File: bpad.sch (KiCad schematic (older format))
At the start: 49 parts, among them J1 USB_B_Mini, SW1 Num, SW10 *, SW11 9, SW12 6, SW13 3, SW14 Del, SW15 -, SW16 +, SW17 Ent, SW2 7, SW3 4, SW4 1, SW5 0, SW6 /, SW7 8, SW8 5, SW9 2, U1 ATmega32U4-AU, Y1 16MHz

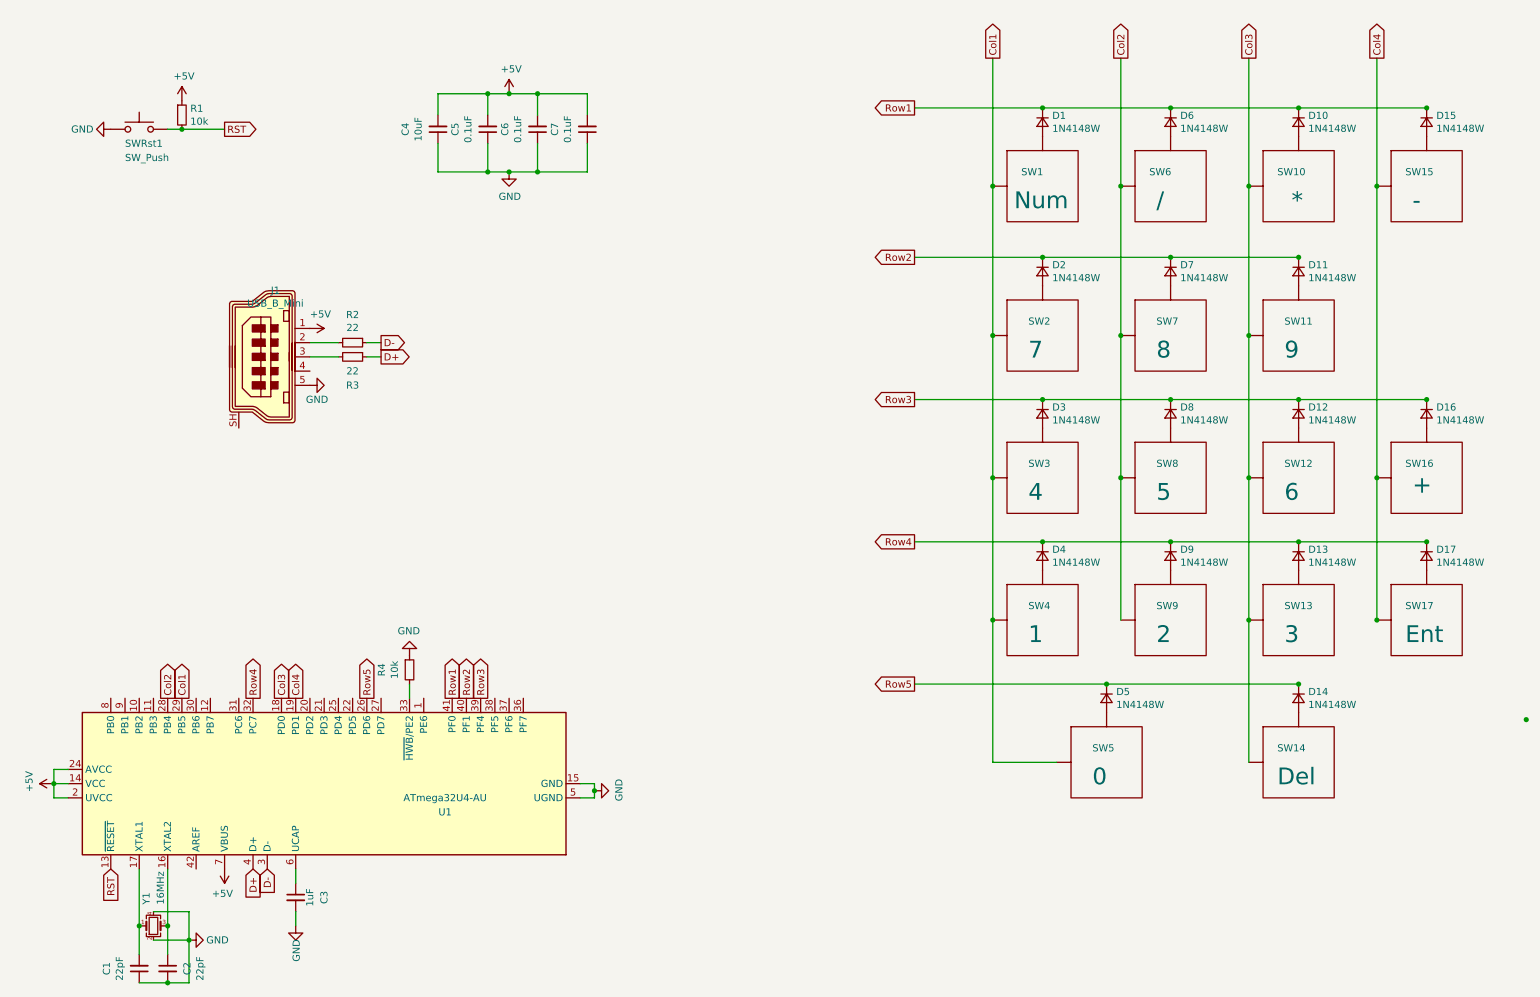
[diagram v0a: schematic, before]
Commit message: started again on the layout
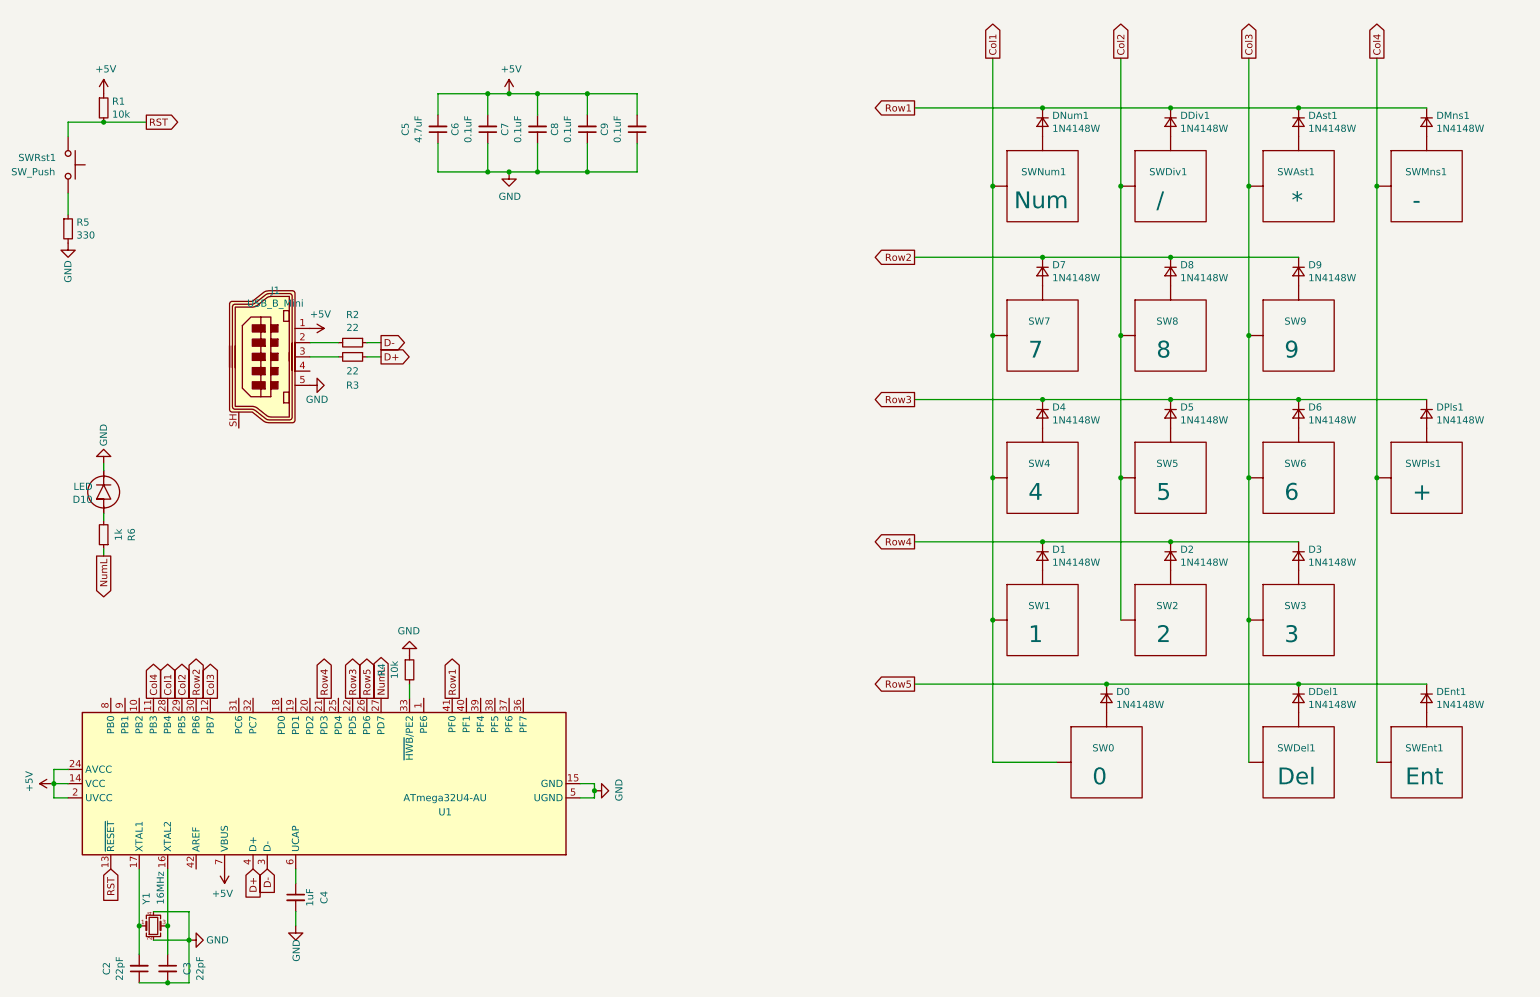
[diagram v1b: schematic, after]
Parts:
- added C9: 0.1uF, Capacitor_SMD:C_0603_1608Metric_Pad1.05x0.95mm_HandSolder, symbol Device:C_Small
- added D10: LED, AcheronComponents:LED_THT_2.54mm, symbol Acheron:LED
- added R5: 330, Resistor_SMD:R_0603_1608Metric_Pad1.05x0.95mm_HandSolder, symbol Device:R_Small
- added R6: 1k, Resistor_SMD:R_0603_1608Metric_Pad1.05x0.95mm_HandSolder, symbol Device:R_Small
- C5: renamed from C4; value 10uF -> 4.7uF
- renumbered C1 to C2, C2 to C3, C3 to C4, C5 to C6, C6 to C7, C7 to C8, D5 to D0, D4 to D1, D9 to D2, D13 to D3, D3 to D4, D8 to D5, D12 to D6, D2 to D7, D7 to D8, D11 to D9, D10 to DAst1, D14 to DDel1, D6 to DDiv1, D17 to DEnt1, D15 to DMns1, D1 to DNum1, D16 to DPls1, SW5 to SW0, SW4 to SW1, SW9 to SW2, SW13 to SW3, SW3 to SW4, SW8 to SW5, SW12 to SW6, SW2 to SW7, SW7 to SW8, SW11 to SW9, SW10 to SWAst1, SW14 to SWDel1, SW6 to SWDiv1, SW17 to SWEnt1, SW15 to SWMns1, SW1 to SWNum1, SW16 to SWPls1
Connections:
- net +5V: now also C9.2
- net Col1: now also U1.28 (PB4); no longer U1.29 (PB5)
- net Col2: now also U1.29 (PB5); no longer U1.28 (PB4)
- net Col3: now also U1.12 (PB7); no longer U1.18 (PD0)
- net Col4: now also U1.11 (PB3); no longer U1.19 (PD1)
- net GND: now also C9.1, D10.K, R5.2; no longer SWRst1.1
- net RST: now also SWRst1.1; no longer SWRst1.2
- net Row2: now also U1.30 (PB6); no longer U1.40 (PF1)
- net Row3: now also U1.22 (PD5); no longer U1.39 (PF4)
- net Row4: now also U1.21 (PD3); no longer DEnt1.1 (K), U1.32 (PC7)
- net Row5: now also DEnt1.1 (K)
- net NumL: now reaches U1.27 (PD7)
- net NumL: now also R6.1
- new net: R5.1, SWRst1.2
- new net: D10.A, R6.2
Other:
- moved on the sheet: DEnt1, R1, SWEnt1, SWRst1

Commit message: moved the usb around and added label
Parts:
- J1: footprint digikey-kicad-library:USB_Mini_B_Female_548190519 -> LocalFootprints:USB_Mini_B_Female_548190519_top
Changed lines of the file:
@@
 F 0 "J1" H 2457 3367 50  0000 C CNN
 F 1 "USB_B_Mini" H 2457 3276 50  0000 C CNN
-F 2 "digikey-kicad-library:USB_Mini_B_Female_548190519" H 2550 2850 50  0001 C CNN
+F 2 "LocalFootprints:USB_Mini_B_Female_548190519_top" H 2550 2850 50  0001 C CNN
 F 3 "~" H 2550 2850 50  0001 C CNN
 	1    2400 2900
